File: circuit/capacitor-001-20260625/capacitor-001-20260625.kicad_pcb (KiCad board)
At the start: 2 copper layers, 32 x 38 mm, 7 parts, among them J1 Conn_01x02_Pin

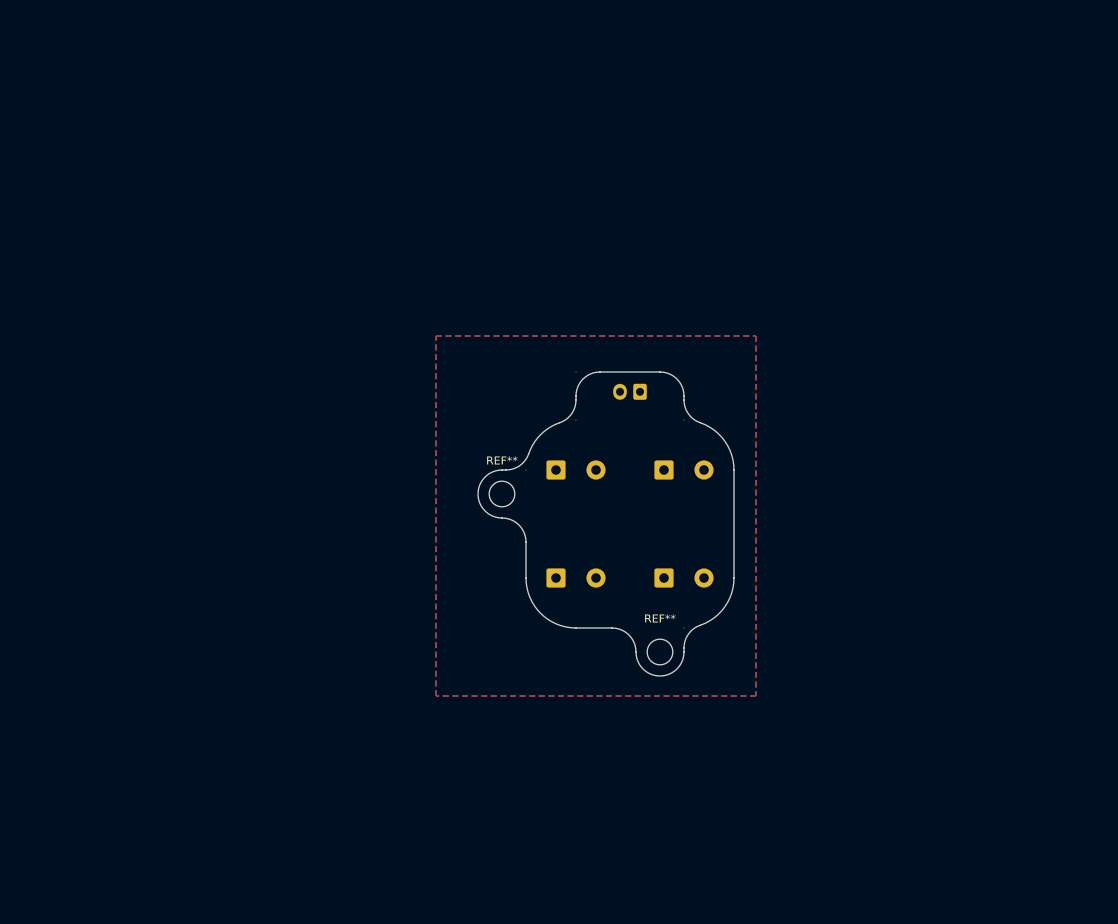
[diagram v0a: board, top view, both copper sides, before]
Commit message: Update コンデンサ基板のボード図を完成させた
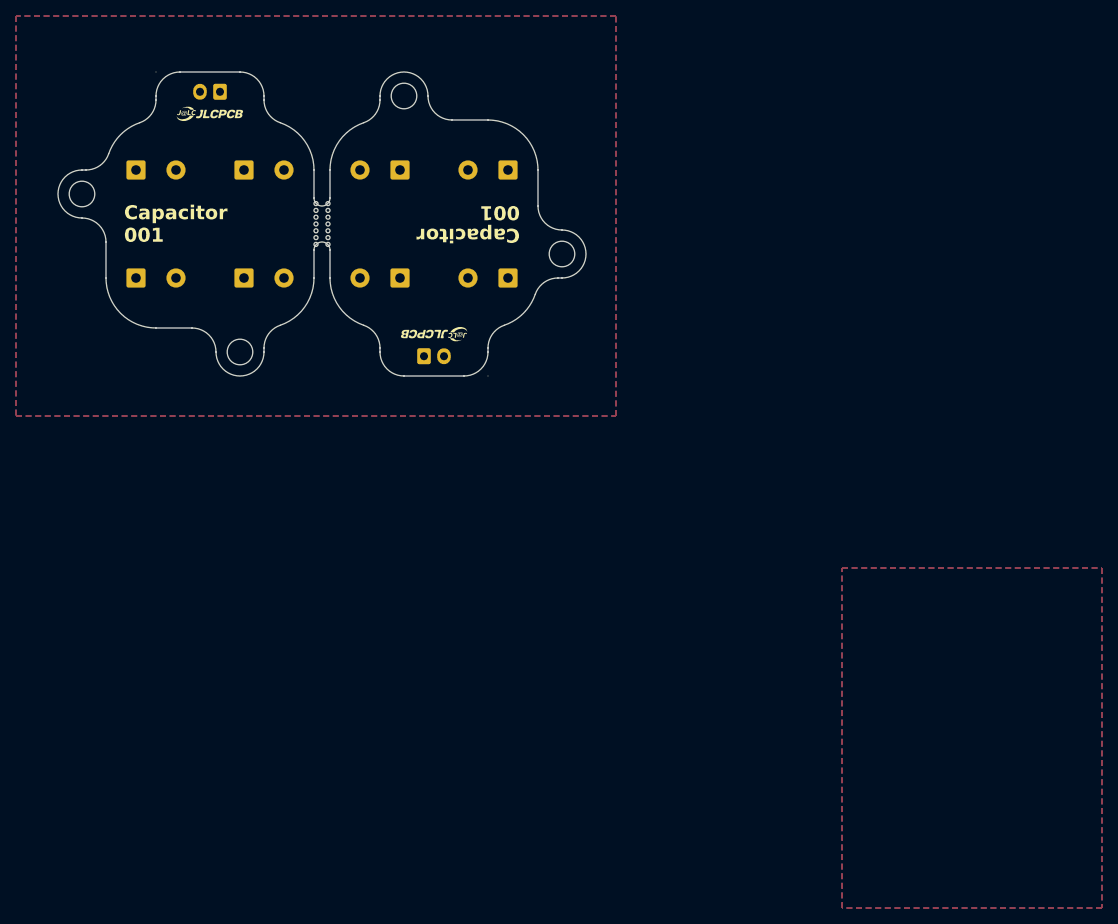
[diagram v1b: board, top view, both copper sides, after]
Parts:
- added C1: 1000u, Capacitor_THT:CP_Radial_D12.5mm_P5.00mm, B.Cu at (76.5, 47.8)
- added C2: 1000u, Capacitor_THT:CP_Radial_D12.5mm_P5.00mm, B.Cu at (63.0, 47.8)
- added C3: 1000u, Capacitor_THT:CP_Radial_D12.5mm_P5.00mm, B.Cu at (76.5, 34.2)
- added C4: 1000u, Capacitor_THT:CP_Radial_D12.5mm_P5.00mm, B.Cu at (63.0, 34.2)
- added J1: Conn_Kicker, Connector_JST:JST_XH_B2B-XH-A_1x02_P2.50mm_Vertical, B.Cu at (66.0, 57.5)
- added REF**: MouseBite-Slot_2.0x4.5mm_outset_D0.5mm_P0.85mm_7h, Panelization:MouseBite-Slot_2.0x4.5mm_outset_D0.5mm_P0.85mm_7h, F.Cu at (52.2, 41.0)
- added REF**: MountingHole_3.2mm_M3, MountingHole:MountingHole_3.2mm_M3, F.Cu at (83.2, 44.8)
- added REF**: MountingHole_3.2mm_M3, MountingHole:MountingHole_3.2mm_M3, F.Cu at (63.5, 25.0)
- J1: value Conn_01x02_Pin -> Conn_Kicker
- moved C1 64.5 mm to (30.0, 34.2)
- moved C2 64.5 mm to (43.5, 34.2)
- moved C3 64.5 mm to (30.0, 47.8)
- moved C4 64.5 mm to (43.5, 47.8)
- moved J1 64.5 mm to (40.5, 24.5)
- moved REF** 64.5 mm to (23.2, 37.2)
- moved REF** 64.5 mm to (43.0, 57.0)
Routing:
- added copper zone on F.Cu, net +48V
- added copper zone on B.Cu, net GND
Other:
- board size 32 x 38 mm -> 66 x 38 mm
- board text added: "Capacitor 001"
